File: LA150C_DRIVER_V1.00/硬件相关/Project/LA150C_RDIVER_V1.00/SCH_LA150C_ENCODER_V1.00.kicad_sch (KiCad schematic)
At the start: 3 parts, among them U4 MT6701

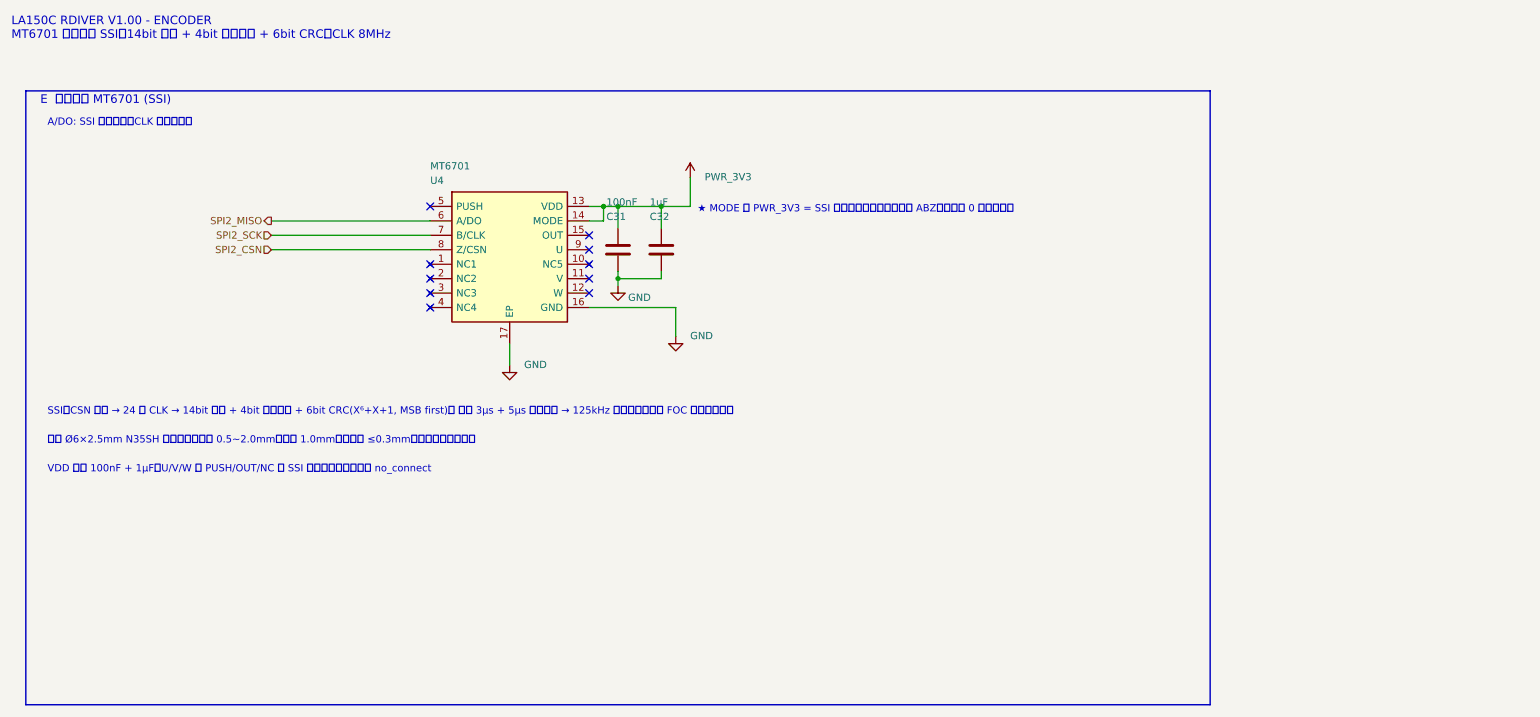
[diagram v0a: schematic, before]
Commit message: feat: finalize LA150C driver schematic
Align the GD32F503 BGA64 pin resources with QS01 V1.12, retain the SCT2230, MT6701 and CAN FD circuits, replace the motor test points with 1.0 x 2.0 mm solder pads, and update the symbols, footprints, ERC report, netlist, BOM and PDF.
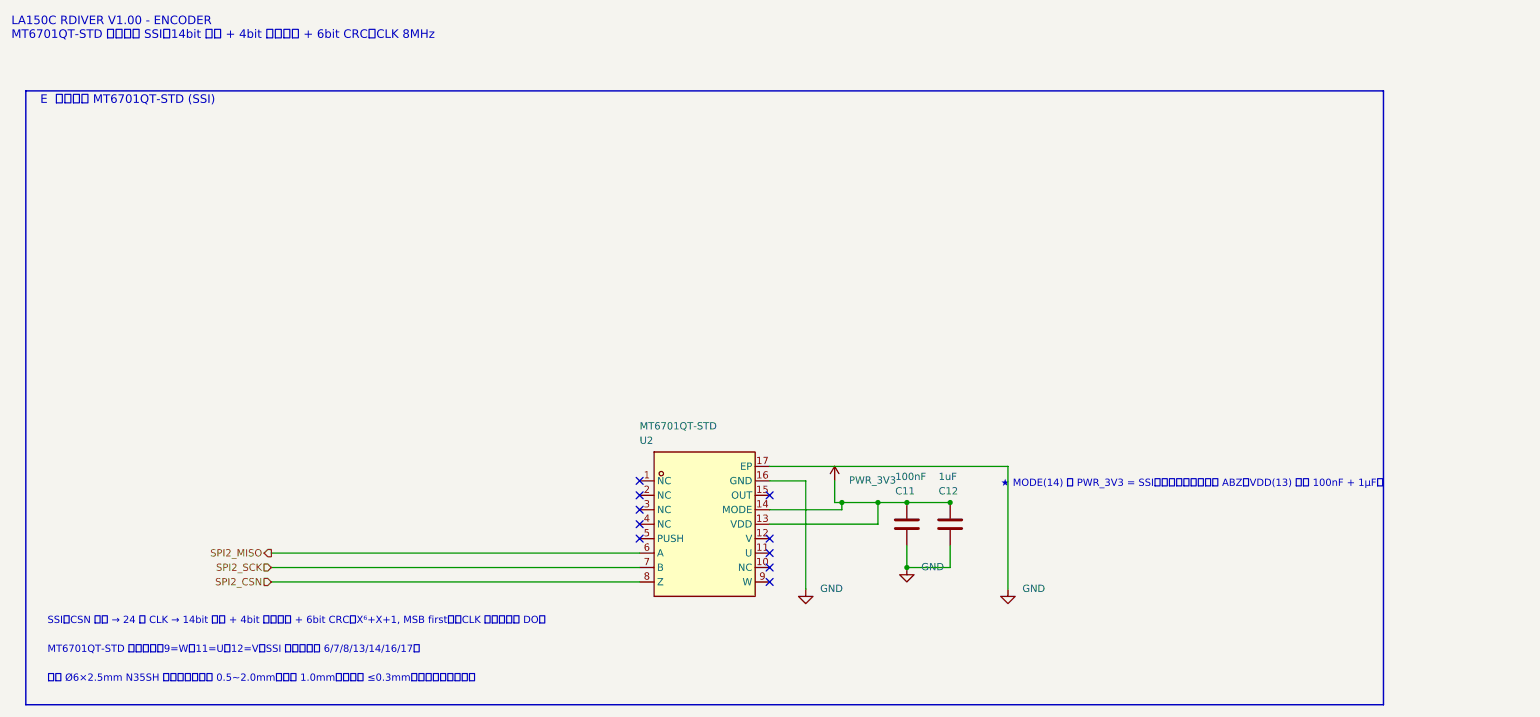
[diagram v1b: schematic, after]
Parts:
- C11: renamed from C31; footprint Capacitors:C_0402_1005Metric -> Capacitors:C0201; symbol LA150C_RDIVER_V1.00:GRM155R71H104KE14D -> LA150C_RDIVER_V1.00:GRM033Z71C104KE14D; LCSC Part C77020 -> C668346; MPN GRM155R71H104KE14D -> GRM033Z71C104KE14D
- C12: renamed from C32; Manufacturer SAMSUNG(三星) -> Samsung Electro-Mechanics
- U2: renamed from U4; value MT6701 -> MT6701QT-STD; footprint (none) -> Magnetic Sensors:VQFN-16_L3.0-W3.0-P0.50-TL-EP1.7; symbol LA150C_RDIVER_V1.00:MT6701 -> LA150C_RDIVER_V1.00:MT6701QT-STD_C2913974; LCSC Part C49257133 -> C2913974; MPN MT6701QT-ACD -> MT6701QT-STD; Manufacturer Magntek -> NOVOSENSE(纳芯微)
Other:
- note added: "E 磁编码器 MT6701QT-STD (SSI)"
- note added: "LA150C RDIVER V1.00 - ENCODER MT6701QT-STD 磁编码器 SSI：14bit 角度 + 4bit 磁场状态 + 6bit CRC，CLK 8MHz"
- note added: "MT6701QT-STD 引脚校正：9=W、11=U、12=V；SSI 模式仅使用 6/7/8/13/14/16/17。"
- note added: "SSI：CSN 拉低 → 24 个 CLK → 14bit 角度 + 4bit 磁场状态 + 6bit CRC（X⁶+X+1, MSB first）；CLK 上升沿更新 DO。"
- note added: "★ MODE(14) 接 PWR_3V3 = SSI；误接地会静默切到 ABZ。VDD(13) 就近 100nF + 1µF。"
- note removed: "A/DO: SSI 数据输出，CLK 上升沿驱动"
- note removed: "E 磁编码器 MT6701 (SSI)"
- note removed: "LA150C RDIVER V1.00 - ENCODER MT6701 磁编码器 SSI：14bit 角度 + 4bit 磁场状态 + 6bit CRC，CLK 8MHz"
- note removed: "SSI：CSN 拉低 → 24 个 CLK → 14bit 角度 + 4bit 磁场状态 + 6bit CRC(X⁶+X+1, MSB first)。 帧长 3µs + 5µs 传播延迟 → 125kHz 更新率，远高于 FOC 电流环需求。"
- note removed: "VDD 去耦 100nF + 1µF；U/V/W 与 PUSH/OUT/NC 在 SSI 模式下不用，全部置 no_connect"
- note removed: "★ MODE 接 PWR_3V3 = SSI 模式；误接地会静默切到 ABZ，读到全 0 或跳变数据"
- moved on the sheet: C11, C12
